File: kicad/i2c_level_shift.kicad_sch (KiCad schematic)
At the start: 4 parts, among them Q3101 NMOS

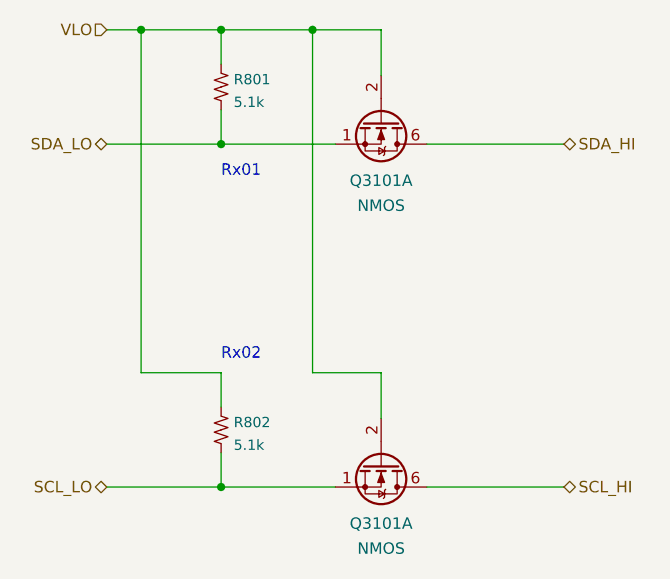
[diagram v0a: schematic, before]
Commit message: Updated part numbers
This sheet is included multiple times, and this time it decided to save with the references from a different instance.
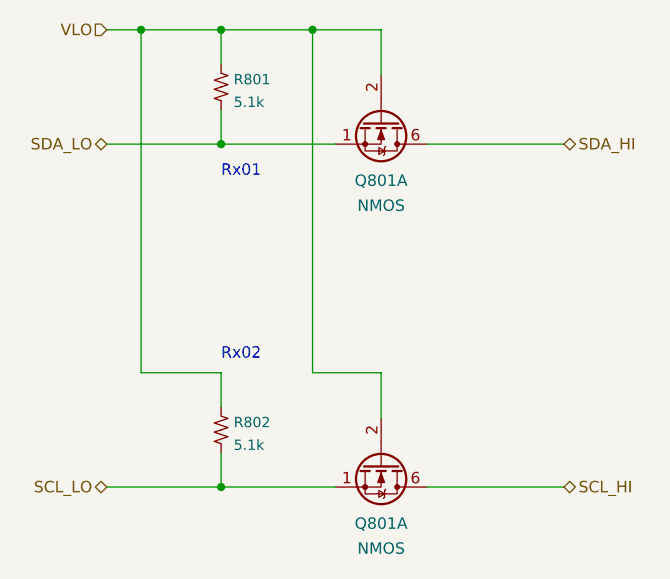
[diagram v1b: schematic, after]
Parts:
- renumbered Q3101 to Q801
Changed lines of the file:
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@@
   (symbol (lib_id "Device:Q_Dual_NMOS_S1G1D2S2G2D1") (at 144.78 124.46 270)
     (in_bom yes) (on_board yes) (fields_autoplaced)
-    (property "Reference" "Q3101" (id 0) (at 144.78 131.0545 90))
+    (property "Reference" "Q801" (id 0) (at 144.78 131.0545 90))
     (property "Value" "NMOS" (id 1) (at 144.78 133.8296 90))
     (property "Footprint" "Package_TO_SOT_SMD:SOT-363_SC-70-6" (id 2) (at 144.78 129.54 0)
@@
   (symbol (lib_id "Device:Q_Dual_NMOS_S1G1D2S2G2D1") (at 144.78 86.36 270)
     (in_bom yes) (on_board yes) (fields_autoplaced)
-    (property "Reference" "Q3101" (id 0) (at 144.78 92.9545 90))
+    (property "Reference" "Q801" (id 0) (at 144.78 92.9545 90))
     (property "Value" "NMOS" (id 1) (at 144.78 95.7296 90))
     (property "Footprint" "Package_TO_SOT_SMD:SOT-363_SC-70-6" (id 2) (at 144.78 91.44 0)

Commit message: Updated Digikey numbers
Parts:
- Q3101: renamed from Q801; Digikey UM6K1NTNCT-ND -> SSM6N24TULFCT-ND
- renumbered R801 to R3101, R802 to R3102
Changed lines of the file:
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@@
   (symbol (lib_id "Device:Q_Dual_NMOS_S1G1D2S2G2D1") (at 144.78 124.46 270)
     (in_bom yes) (on_board yes) (fields_autoplaced)
-    (property "Reference" "Q801" (id 0) (at 144.78 131.0545 90))
+    (property "Reference" "Q3101" (id 0) (at 144.78 131.0545 90))
     (property "Value" "NMOS" (id 1) (at 144.78 133.8296 90))
     (property "Footprint" "Package_TO_SOT_SMD:SOT-363_SC-70-6" (id 2) (at 144.78 129.54 0)
@@
       (effects (font (size 1.27 1.27)) hide)
     )
-    (property "Digikey" "UM6K1NTNCT-ND" (id 4) (at 144.78 124.46 0)
+    (property "Digikey" "SSM6N24TULFCT-ND" (id 4) (at 144.78 124.46 0)
       (effects (font (size 1.27 1.27)) hide)
     )
@@
   (symbol (lib_id "KwanSystems:RESISTOR") (at 127 82.55 90)
     (in_bom yes) (on_board yes) (fields_autoplaced)
-    (property "Reference" "R801" (id 0) (at 128.397 81.7197 90)
+    (property "Reference" "R3101" (id 0) (at 128.397 81.7197 90)
       (effects (font (size 1.143 1.143)) (justify right))
     )
@@
   (symbol (lib_id "KwanSystems:RESISTOR") (at 127 120.65 90)
     (in_bom yes) (on_board yes) (fields_autoplaced)
-    (property "Reference" "R802" (id 0) (at 128.397 119.8197 90)
+    (property "Reference" "R3102" (id 0) (at 128.397 119.8197 90)
       (effects (font (size 1.143 1.143)) (justify right))
     )
@@
   (symbol (lib_id "Device:Q_Dual_NMOS_S1G1D2S2G2D1") (at 144.78 86.36 270)
     (in_bom yes) (on_board yes) (fields_autoplaced)
-    (property "Reference" "Q801" (id 0) (at 144.78 92.9545 90))
+    (property "Reference" "Q3101" (id 0) (at 144.78 92.9545 90))
     (property "Value" "NMOS" (id 1) (at 144.78 95.7296 90))
     (property "Footprint" "Package_TO_SOT_SMD:SOT-363_SC-70-6" (id 2) (at 144.78 91.44 0)
@@
       (effects (font (size 1.27 1.27)) hide)
     )
-    (property "Digikey" "UM6K1NTNCT-ND" (id 4) (at 144.78 86.36 0)
+    (property "Digikey" "SSM6N24TULFCT-ND" (id 4) (at 144.78 86.36 0)
       (effects (font (size 1.27 1.27)) hide)
     )

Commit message: Checkin before branch
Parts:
- renumbered Q3101 to Q1601, R3101 to R1601, R3102 to R1602
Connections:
- net SCL_HI: now also Q1601.6 (D); no longer Q1601.6 (D)
- net SCL_LO: now also Q1601.1 (S); no longer Q1601.1 (S)
- net SDA_HI: now also Q1601.6 (D); no longer Q1601.6 (D)
- net SDA_LO: now also Q1601.1 (S); no longer Q1601.1 (S)
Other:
- moved on the sheet: Q1601A
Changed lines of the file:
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@@
     (effects (font (size 1.27 1.27)) (justify left))
   )
-  (symbol (lib_id "Device:Q_Dual_NMOS_S1G1D2S2G2D1") (at 144.78 124.46 270)
+  (symbol (lib_id "Device:Q_Dual_NMOS_S1G1D2S2G2D1") (at 144.78 86.36 270)
     (in_bom yes) (on_board yes) (fields_autoplaced)
-    (property "Reference" "Q3101" (id 0) (at 144.78 131.0545 90))
-    (property "Value" "NMOS" (id 1) (at 144.78 133.8296 90))
-    (property "Footprint" "Package_TO_SOT_SMD:SOT-363_SC-70-6" (id 2) (at 144.78 129.54 0)
+    (property "Reference" "Q1601" (id 0) (at 144.78 92.8354 90))
+    (property "Value" "NMOS" (id 1) (at 144.78 95.3723 90))
+    (property "Footprint" "Package_TO_SOT_SMD:SOT-363_SC-70-6" (id 2) (at 144.78 91.44 0)
       (effects (font (size 1.27 1.27)) hide)
     )
-    (property "Datasheet" "~" (id 3) (at 144.78 129.54 0)
+    (property "Datasheet" "~" (id 3) (at 144.78 91.44 0)
       (effects (font (size 1.27 1.27)) hide)
     )
-    (property "Digikey" "SSM6N24TULFCT-ND" (id 4) (at 144.78 124.46 0)
+    (property "Digikey" "SSM6N24TULFCT-ND" (id 4) (at 144.78 86.36 0)
       (effects (font (size 1.27 1.27)) hide)
     )
-    (property "Purpose" "I2C level shift" (id 5) (at 144.78 124.46 0)
+    (property "Purpose" "I2C level shift" (id 5) (at 144.78 86.36 0)
       (effects (font (size 1.27 1.27)) hide)
     )
@@
   (symbol (lib_id "KwanSystems:RESISTOR") (at 127 82.55 90)
     (in_bom yes) (on_board yes) (fields_autoplaced)
-    (property "Reference" "R3101" (id 0) (at 128.397 81.7197 90)
+    (property "Reference" "R1601" (id 0) (at 128.397 81.7861 90)
       (effects (font (size 1.143 1.143)) (justify right))
     )
-    (property "Value" "5.1k" (id 1) (at 128.397 84.2425 90)
+    (property "Value" "5.1k" (id 1) (at 128.397 84.0947 90)
       (effects (font (size 1.143 1.143)) (justify right))
     )
@@
   (symbol (lib_id "KwanSystems:RESISTOR") (at 127 120.65 90)
     (in_bom yes) (on_board yes) (fields_autoplaced)
-    (property "Reference" "R3102" (id 0) (at 128.397 119.8197 90)
+    (property "Reference" "R1602" (id 0) (at 128.397 119.8861 90)
       (effects (font (size 1.143 1.143)) (justify right))
     )
-    (property "Value" "5.1k" (id 1) (at 128.397 122.3425 90)
+    (property "Value" "5.1k" (id 1) (at 128.397 122.1947 90)
       (effects (font (size 1.143 1.143)) (justify right))
     )
@@
     (pin "2")
   )
-  (symbol (lib_id "Device:Q_Dual_NMOS_S1G1D2S2G2D1") (at 144.78 86.36 270)
+  (symbol (lib_id "Device:Q_Dual_NMOS_S1G1D2S2G2D1") (at 144.78 124.46 270)
     (in_bom yes) (on_board yes) (fields_autoplaced)
-    (property "Reference" "Q3101" (id 0) (at 144.78 92.9545 90))
-    (property "Value" "NMOS" (id 1) (at 144.78 95.7296 90))
-    (property "Footprint" "Package_TO_SOT_SMD:SOT-363_SC-70-6" (id 2) (at 144.78 91.44 0)
+    (property "Reference" "Q1601" (id 0) (at 144.78 130.9354 90))
+    (property "Value" "NMOS" (id 1) (at 144.78 133.4723 90))
+    (property "Footprint" "Package_TO_SOT_SMD:SOT-363_SC-70-6" (id 2) (at 144.78 129.54 0)
       (effects (font (size 1.27 1.27)) hide)
     )
-    (property "Datasheet" "~" (id 3) (at 144.78 91.44 0)
+    (property "Datasheet" "~" (id 3) (at 144.78 129.54 0)
       (effects (font (size 1.27 1.27)) hide)
     )
-    (property "Digikey" "SSM6N24TULFCT-ND" (id 4) (at 144.78 86.36 0)
+    (property "Digikey" "SSM6N24TULFCT-ND" (id 4) (at 144.78 124.46 0)
       (effects (font (size 1.27 1.27)) hide)
     )
-    (property "Purpose" "I2C level shift" (id 5) (at 144.78 86.36 0)
+    (property "Purpose" "I2C level shift" (id 5) (at 144.78 124.46 0)
       (effects (font (size 1.27 1.27)) hide)
     )
